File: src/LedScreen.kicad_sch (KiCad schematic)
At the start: 38 parts

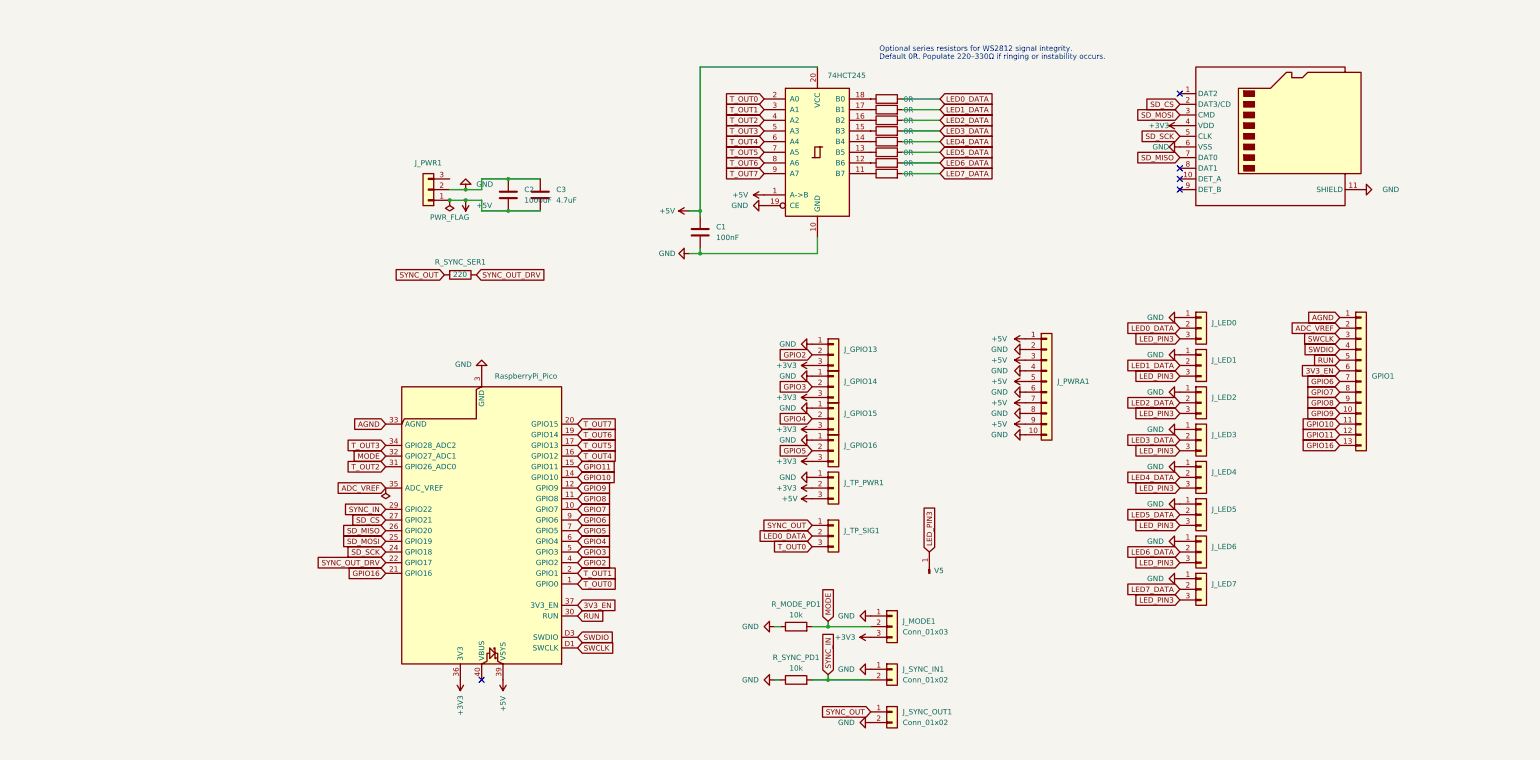
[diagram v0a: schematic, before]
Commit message: Reorganize KiCad project layout
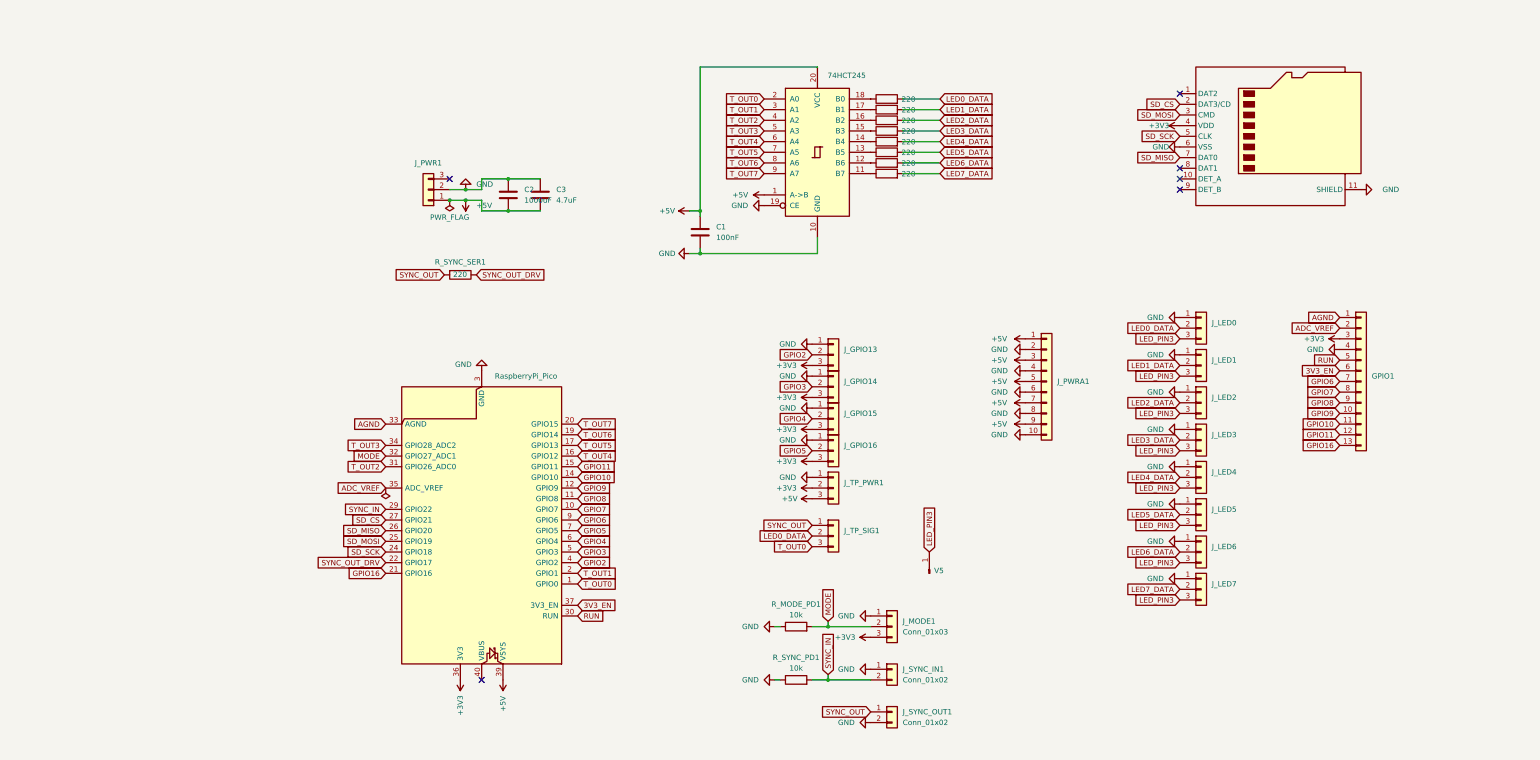
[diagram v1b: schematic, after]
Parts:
- A1: symbol MCU_Module:RaspberryPi_Pico_Debug -> MCU_Module:RaspberryPi_Pico
- R1, R2, R3, R4, R5, R6, R7, R8: value 0R -> 220
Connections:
- net +3V3: now also GPIO1.3 (Pin_3)
- net GND: now also GPIO1.4 (Pin_4); no longer A1.D2 (GND)
- removed net SWCLK: A1.D1 (SWCLK), GPIO1.3 (Pin_3)
- removed net SWDIO: A1.D3 (SWDIO), GPIO1.4 (Pin_4)
- no-connect marks 5 -> 6
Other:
- note removed: "Default 0R. Populate 220–330Ω if ringing or instability occurs."
- note removed: "Optional series resistors for WS2812 signal integrity."
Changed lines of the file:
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@@
 		(comment 1 "Ruben Straks")
 	)
-	(text "Default 0R. Populate 220–330Ω if ringing or instability occurs."
-		(exclude_from_sim no)
-		(at 148.082 29.464 0)
-		(effects
-			(font
-				(size 1.27 1.27)
-			)
-			(justify left)
-		)
-	)
-	(text "Optional series resistors for WS2812 signal integrity."
-		(exclude_from_sim no)
-		(at 148.082 27.559 0)
-		(effects
-			(font
-				(size 1.27 1.27)
-			)
-			(justify left)
-		)
-	)
 	(junction
 		(at 105.41 76.2)
@@
 	)
 	(no_connect
+		(at 45.72 58.42)
+	)
+	(no_connect
 		(at 219.71 58.42)
 	)
@@
 		)
 	)
-	(global_label "SWCLK"
-		(shape input)
-		(at 257.81 96.52 180)
-		(fields_autoplaced yes)
-		(effects
-			(font
-				(size 1.27 1.27)
-			)
-			(justify right)
-		)
-		(property "Intersheetrefs" "${INTERSHEET_REFS}"
-			(at 248.5958 96.52 0)
-			(effects
-				(font
-					(size 1.27 1.27)
-				)
-				(justify right)
-				(hide yes)
-			)
-		)
-	)
 	(global_label "3V3_EN"
 		(shape input)
@@
 		)
 	)
-	(global_label "SWCLK"
-		(shape input)
-		(at 76.2 170.18 0)
-		(fields_autoplaced yes)
-		(effects
-			(font
-				(size 1.27 1.27)
-			)
-			(justify left)
-		)
-		(property "Intersheetrefs" "${INTERSHEET_REFS}"
-			(at 85.4142 170.18 0)
-			(effects
-				(font
-					(size 1.27 1.27)
-				)
-				(justify left)
-				(hide yes)
-			)
-		)
-	)
 	(global_label "MODE"
 		(shape input)
@@
 		)
 	)
-	(global_label "SWDIO"
-		(shape input)
-		(at 76.2 167.64 0)
-		(fields_autoplaced yes)
-		(effects
-			(font
-				(size 1.27 1.27)
-			)
-			(justify left)
-		)
-		(property "Intersheetrefs" "${INTERSHEET_REFS}"
-			(at 85.0514 167.64 0)
-			(effects
-				(font
-					(size 1.27 1.27)
-				)
-				(justify left)
-				(hide yes)
-			)
-		)
-	)
 	(global_label "GPIO16"
 		(shape input)
@@
 		)
 	)
-	(global_label "SWDIO"
-		(shape input)
-		(at 257.81 99.06 180)
-		(fields_autoplaced yes)
-		(effects
-			(font
-				(size 1.27 1.27)
-			)
-			(justify right)
-		)
-		(property "Intersheetrefs" "${INTERSHEET_REFS}"
-			(at 248.9586 99.06 0)
-			(effects
-				(font
-					(size 1.27 1.27)
-				)
-				(justify right)
-				(hide yes)
-			)
-		)
-	)
 	(symbol
 		(lib_id "power:GND")
@@
 			)
 		)
-		(property "Value" "0R"
+		(property "Value" "220"
 			(at 155.0476 47.0572 90)
 			(effects
@@
 			)
 		)
-		(property "Value" "0R"
+		(property "Value" "220"
 			(at 155.0476 49.5972 90)
 			(effects
@@
 			)
 		)
-		(property "Value" "0R"
+		(property "Value" "220"
 			(at 155.0476 41.9772 90)
 			(effects
@@
 	)
 	(symbol
-		(lib_id "MCU_Module:RaspberryPi_Pico_Debug")
+		(lib_id "MCU_Module:RaspberryPi_Pico")
 		(at 53.34 139.7 180)
 		(unit 1)
@@
 			)
 		)
-		(property "Description" "Versatile and inexpensive microcontroller module (with debug pins) powered by RP2040 dual-core Arm Cortex-M0+ processor up to 133 MHz, 264kB SRAM, 2MB QSPI flash; also supports Raspberry Pi Pico 2"
+		(property "Description" "Versatile and inexpensive microcontroller module powered by RP2040 dual-core Arm Cortex-M0+ processor up to 133 MHz, 264kB SRAM, 2MB QSPI flash; also supports Raspberry Pi Pico 2"
 			(at 53.34 87.63 0)
 			(effects
@@
 		(pin "27"
 		)
-		(pin "D2"
-		)
 		(pin "36"
 		)
@@
 		(pin "30"
 		)
-		(pin "D3"
-		)
-		(pin "D1"
-		)
 		(pin "28"
 		)
@@
 	)
 	(symbol
+		(lib_id "power:+3V3")
+		(at 257.81 96.52 90)
+		(unit 1)
+		(exclude_from_sim no)
+		(in_bom yes)
+		(on_board yes)
+		(dnp no)
+		(property "Reference" "#PWR023"
+			(at 261.62 96.52 0)
+			(effects
+				(font
+					(size 1.27 1.27)
+				)
+				(hide yes)
+			)
+		)
+		(property "Value" "+3V3"
+			(at 251.714 96.52 90)
+			(effects
+				(font
+					(size 1.27 1.27)
+				)
+			)
+		)
+		(property "Footprint" ""
+			(at 257.81 96.52 0)
+			(effects
+				(font
+					(size 1.27 1.27)
+				)
+				(hide yes)
+			)
+		)
+		(property "Datasheet" ""
+			(at 257.81 96.52 0)
+			(effects
+				(font
+					(size 1.27 1.27)
+				)
+				(hide yes)
+			)
+		)
+		(property "Description" "Power symbol creates a global label with name \"+3V3\""
+			(at 257.81 96.52 0)
+			(effects
+				(font
+					(size 1.27 1.27)
+				)
+				(hide yes)
+			)
+		)
+		(pin "1"
+		)
+		(instances
+			(project "LedScreen"
+				(path "/6393ae6b-20d3-4709-8a4f-a83a956b3492"
+					(reference "#PWR023")
+					(unit 1)
+				)
+			)
+		)
+	)
+	(symbol
 		(lib_id "power:+5V")
 		(at 102.87 66.04 90)
@@
 			)
 		)
-		(property "Value" "0R"
+		(property "Value" "220"
 			(at 155.0476 52.1372 90)
 			(effects
@@
 			)
 		)
-		(property "Value" "0R"
+		(property "Value" "220"
 			(at 155.0476 54.6772 90)
 			(effects
@@
 			)
 		)
-		(property "Value" "0R"
+		(property "Value" "220"
 			(at 155.0476 57.2172 90)
 			(effects
@@
 			)
 		)
-		(property "Value" "0R"
+		(property "Value" "220"
 			(at 155.0476 44.5172 90)
 			(effects
@@
 	)
 	(symbol
+		(lib_id "power:GND")
+		(at 257.81 99.06 270)
+		(unit 1)
+		(exclude_from_sim no)
+		(in_bom yes)
+		(on_board yes)
+		(dnp no)
+		(fields_autoplaced yes)
+		(property "Reference" "#PWR03"
+			(at 251.46 99.06 0)
+			(effects
+				(font
+					(size 1.27 1.27)
+				)
+				(hide yes)
+			)
+		)
+		(property "Value" "GND"
+			(at 254 99.0599 90)
+			(effects
+				(font
+					(size 1.27 1.27)
+				)
+				(justify right)
+			)
+		)
+		(property "Footprint" ""
+			(at 257.81 99.06 0)
+			(effects
+				(font
+					(size 1.27 1.27)
+				)
+				(hide yes)
+			)
+		)
+		(property "Datasheet" ""
+			(at 257.81 99.06 0)
+			(effects
+				(font
+					(size 1.27 1.27)
+				)
+				(hide yes)
+			)
+		)
+		(property "Description" "Power symbol creates a global label with name \"GND\" , ground"
+			(at 257.81 99.06 0)
+			(effects
+				(font
+					(size 1.27 1.27)
+				)
+				(hide yes)
+			)
+		)
+		(pin "1"
+		)
+		(instances
+			(project "LedScreen"
+				(path "/6393ae6b-20d3-4709-8a4f-a83a956b3492"
+					(reference "#PWR03")
+					(unit 1)
+				)
+			)
+		)
+	)
+	(symbol
 		(lib_id "Device:R")
 		(at 149.86 39.37 90)
@@
 			)
 		)
-		(property "Value" "0R"
+		(property "Value" "220"
 			(at 155.0476 39.4372 90)
 			(effects
